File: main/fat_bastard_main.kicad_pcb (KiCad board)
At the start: 2 copper layers, 195 x 50 mm, 54 parts, among them J1 INPUT, J2 TO_LD_12V, J3 TO_LD_IN, J4 TO_LD_GAIN, J5 TO_LD_OUT, J6 12V_IN, J8 FOOTSW, J9 OUTPUT, K1 FINDER-30.22, U1 OPA2134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

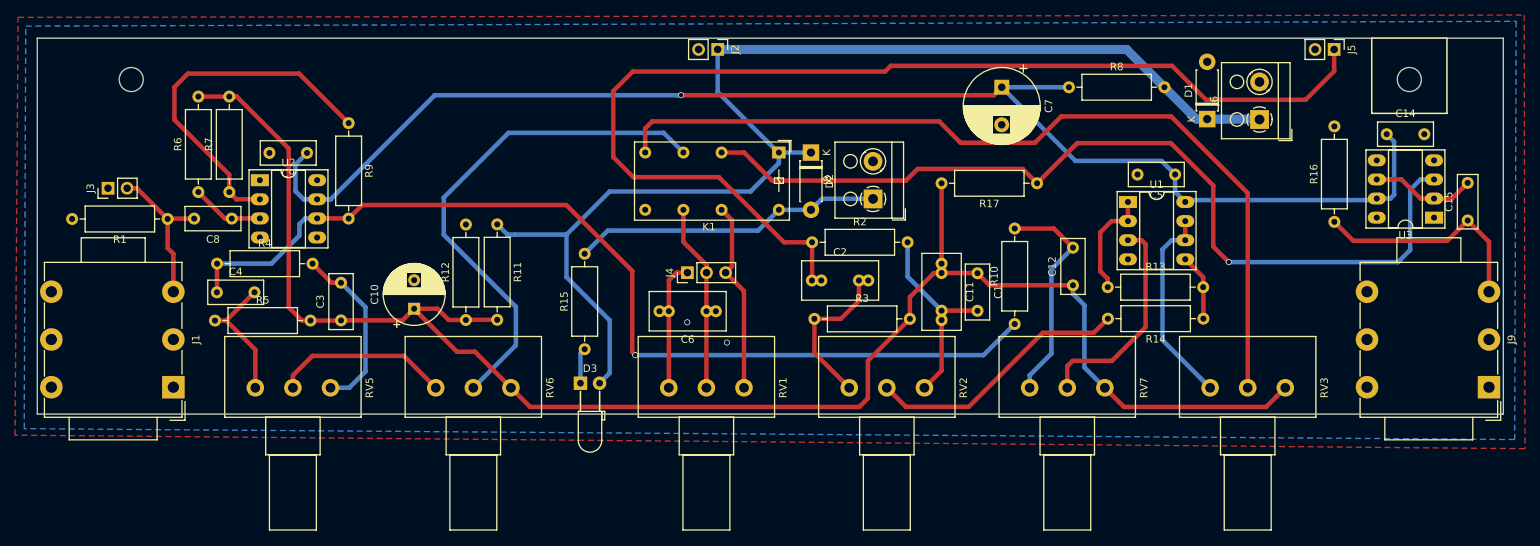
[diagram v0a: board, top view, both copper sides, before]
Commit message: [main] Attenuate lead channel & improve buffering + final PCB
Lead channel has a high output level, while the signal level after the
Depth control is quite low. Therfore, we need to attenuate the lead
channel before trying to mix in the signal coming from the Depth pot.

Additionnally, the output buffer is changed to a make-up gain stage.

With these changes in mind, the PCB design has been completed.
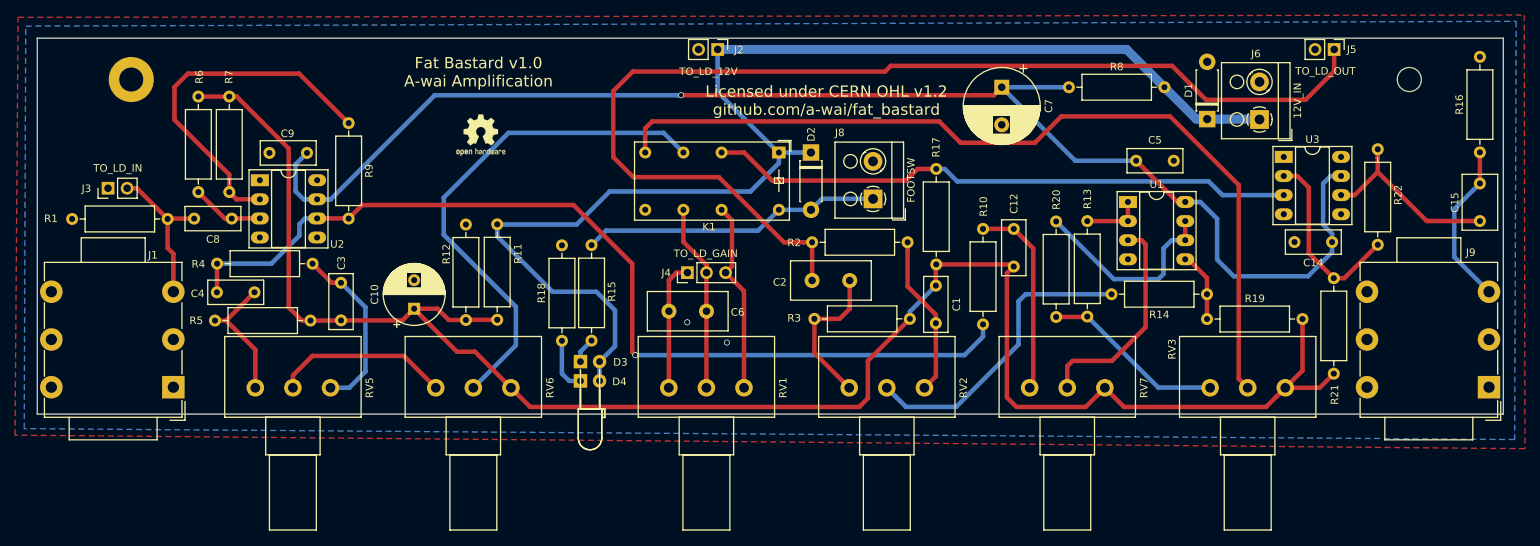
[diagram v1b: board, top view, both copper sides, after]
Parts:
- removed C11: 500p, Capacitor_THT:C_Rect_L10.0mm_W5.0mm_P5.00mm_P7.50mm
- removed the DRILL at (62.5, 65.5)
- added D4: PWR, LED_THT:LED_D3.0mm_Horizontal_O3.81mm_Z2.0mm, F.Cu at (122.3, 105.6)
- added R18: 1.8k, Resistor_THT:R_Axial_DIN0309_L9.0mm_D3.2mm_P12.70mm_Horizontal, F.Cu at (119.8, 100.3)
- added R19: 47k, Resistor_THT:R_Axial_DIN0309_L9.0mm_D3.2mm_P12.70mm_Horizontal, F.Cu at (205.6, 97.4)
- added R20: 10k, Resistor_THT:R_Axial_DIN0309_L9.0mm_D3.2mm_P12.70mm_Horizontal, F.Cu at (185.5, 84.4)
- added R21: 1k, Resistor_THT:R_Axial_DIN0309_L9.0mm_D3.2mm_P12.70mm_Horizontal, F.Cu at (222.5, 104.6)
- added R22: 4.7k, Resistor_THT:R_Axial_DIN0309_L9.0mm_D3.2mm_P12.70mm_Horizontal, F.Cu at (228.3, 87.5)
- added REF**: MountingHole_3.2mm_M3, MountingHole:MountingHole_3.2mm_M3, F.Cu at (62.5, 65.5)
- added REF**: OSHW-Logo2_7.3x6mm_SilkScreen, Symbol:OSHW-Logo2_7.3x6mm_SilkScreen, F.Cu at (109.0, 72.9)
- C1: value 1n -> 1.5n
- C12: value 100n -> 220n
- C15: footprint Capacitor_THT:C_Rect_L7.0mm_W2.5mm_P5.00mm -> Capacitor_THT:C_Rect_L7.2mm_W4.5mm_P5.00mm_FKS2_FKP2_MKS2_MKP2
- C2, C6: footprint Capacitor_THT:C_Rect_L10.0mm_W5.0mm_P5.00mm_P7.50mm -> Capacitor_THT:C_Disc_D10.5mm_W5.0mm_P5.00mm
- D3: value LED -> LEAD; footprint LED_THT:LED_D3.0mm_Horizontal_O3.81mm_Z6.0mm -> LED_THT:LED_D3.0mm_Horizontal_O6.35mm_Z10.0mm
- R10: value 8.2k -> 6.8k
- R13: value 470k -> 10k
- R14: value 470k -> 1M
- R15: value 3.3k -> 1.8k
- R9: value 10k -> 3.9k
- moved U3 21.6 mm to (215.8, 75.8), turned to 0 degrees
- moved R16 21.4 mm to (241.9, 75.2)
- moved C14 16.1 mm to (222.2, 87.1), turned to 180 degrees
- moved R17 13.5 mm to (169.6, 77.4), turned to 270 degrees
- moved C12 8.26 mm to (179.9, 90.4)
- moved C1 5.78 mm to (169.5, 92.9)
- moved C5 5.49 mm to (196.2, 76.3), turned to 0 degrees
- moved C15 5.19 mm to (241.9, 79.3), turned to 270 degrees
- moved R13 4.76 mm to (189.7, 97.0), turned to 90 degrees
- moved R10 4.22 mm to (175.8, 98.1)
- moved R14 3.29 mm to (205.6, 94.1)
- moved D3 2.87 mm to (122.2, 103.0)
- moved R15 1.46 mm to (123.7, 100.2)
- moved C6 1.24 mm to (139.0, 96.3)
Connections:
- R14 pad 1: Net-(R13-Pad2) -> Net-(R14-Pad1)
- RV3 pad 1: Net-(RV3-Pad1) -> Net-(R13-Pad1)
- U1 pad 1: Net-(R13-Pad1) -> Net-(R13-Pad2)
- U1 pad 2: Net-(R13-Pad1) -> Net-(R13-Pad2)
- U1 pad 5: Net-(R13-Pad2) -> Net-(R14-Pad1)
- U1 pad 6: Net-(RV3-Pad1) -> Net-(R20-Pad1)
- U1 pad 7: Net-(RV3-Pad1) -> Net-(R20-Pad1)
- U3 pad 2: Net-(C15-Pad2) -> Net-(R21-Pad2)
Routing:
- net Net-(K1-Pad11): track 120.5 -> 78.4 mm, vias 1 -> 0
- net Net-(RV3-Pad1): track 27.1 -> 0.00 mm
- net Net-(R20-Pad1): track 0.00 -> 27.0 mm
- net Net-(R21-Pad2): track 0.00 -> 25.1 mm
- net GNDS: track 224.9 -> 239.8 mm
- net Net-(C15-Pad2): track 14.0 -> 25.5 mm
- net Net-(R13-Pad1): track 14.5 -> 24.4 mm
- net Net-(R14-Pad1): track 0.00 -> 9.38 mm
- net Net-(C15-Pad1): track 30.5 -> 21.9 mm
- net +12V: track 163.6 -> 171.4 mm
- net Net-(D4-Pad1): track 0.00 -> 7.23 mm
- net Net-(C1-Pad2): track 27.0 -> 21.5 mm
- net Net-(R14-Pad2): track 35.3 -> 40.5 mm
- net Net-(C12-Pad2): track 29.8 -> 26.5 mm
- net Net-(C4-Pad1): track 130.4 -> 127.6 mm
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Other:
- board text added: "Fat Bastard v1.0 A-wai Amplification"
- board text added: "Licensed under CERN OHL v1.2 github.com/a-wai/fat_bastard"

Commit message: Make main-alt PCB the only main PCB
Signed-off-by: Arnaud Ferraris <arnaud.ferraris@gmail.com>
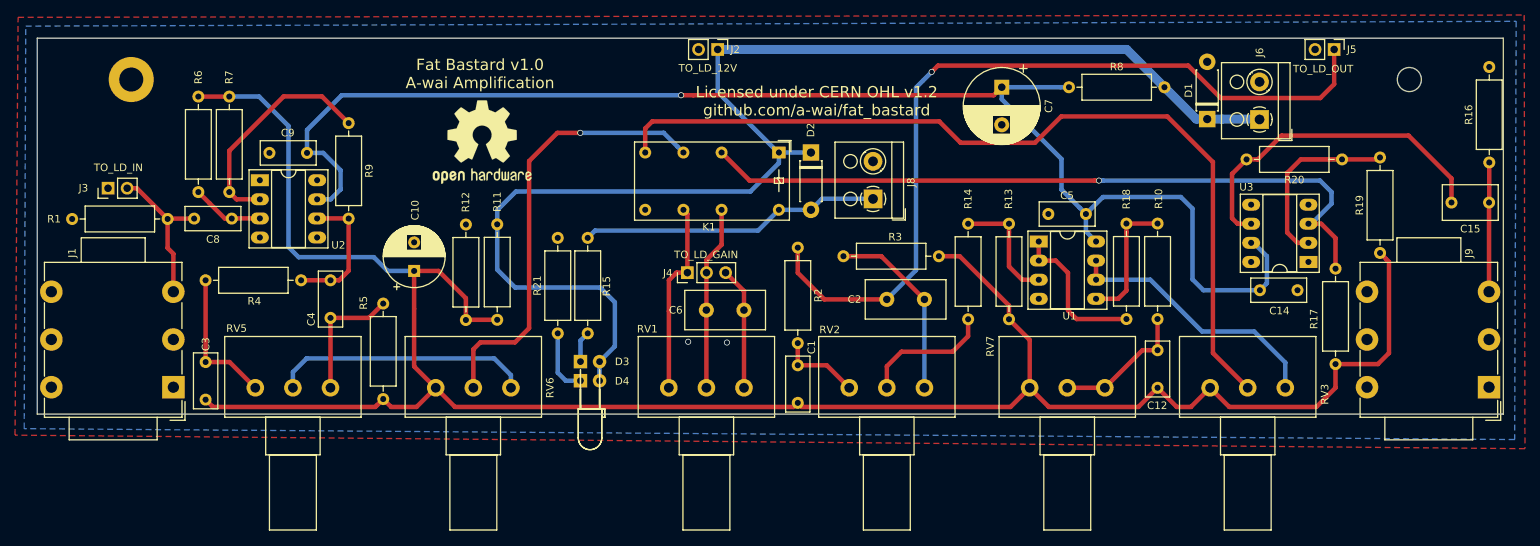
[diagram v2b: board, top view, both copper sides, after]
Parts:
- removed R22: 4.7k, Resistor_THT:R_Axial_DIN0309_L9.0mm_D3.2mm_P12.70mm_Horizontal
- removed the REF** at (62.5, 65.5)
- removed the REF** at (109.0, 72.9)
- added DRILL: MountingHole_3.2mm_M3, MountingHole:MountingHole_3.2mm_M3, F.Cu at (62.5, 65.5)
- added REF**: OSHW-Logo2_14.6x12mm_SilkScreen, Symbol:OSHW-Logo2_14.6x12mm_SilkScreen, F.Cu at (109.2, 73.8)
- C12: value 220n -> 10n
- R1: value 1M -> 2.2M
- R10: value 6.8k -> 33k
- R13: value 10k -> 47k
- R18: value 1.8k -> 330k
- R19: value 47k -> 1k
- R20: value 10k -> 3.3k
- R21: value 1k -> 1.8k
- R9: value 3.9k -> 2.2k
- RV7: value 100k-A -> 1M-A
- moved R21 103.4 mm to (119.2, 99.3)
- moved R18 75.1 mm to (194.9, 97.4)
- moved R17 54.7 mm to (222.7, 90.7)
- moved R20 38.9 mm to (223.5, 76.1), turned to 180 degrees
- moved R14 31.9 mm to (173.8, 97.4), turned to 90 degrees
- moved R10 26.8 mm to (199.0, 84.7), turned to 270 degrees
- moved C12 25.0 mm to (199.0, 106.5)
- moved R19 24.6 mm to (228.6, 88.6), turned to 90 degrees
- moved C1 24.1 mm to (151.2, 108.5), turned to 90 degrees
- moved R5 22.5 mm to (96.0, 95.3), turned to 270 degrees
- moved C3 20.9 mm to (72.4, 108.1)
- moved R13 16.2 mm to (179.2, 84.7), turned to 270 degrees
- moved C4 15.2 mm to (89.0, 92.2), turned to 270 degrees
- moved U3 14.3 mm to (219.1, 89.8), turned to 180 degrees
- moved U1 13.0 mm to (183.2, 87.0)
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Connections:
- J4 pad 1: Net-(C6-Pad2) -> /LD_GND
- J4 pad 3: /LD_GND -> Net-(C6-Pad2)
- K1 pad 21: /LD_GND -> /LD_SIG
- K1 pad 22: /LD_SIG -> /LD_GND
- R10 pad 1: Net-(C4-Pad1) -> Net-(R10-Pad1)
- R13 pad 2: Net-(R13-Pad2) -> GNDS
- R14 pad 2: Net-(R14-Pad2) -> Net-(R13-Pad1)
- R18 pad 1: Net-(D4-Pad1) -> Net-(R18-Pad1)
- R18 pad 2: GND -> Net-(R10-Pad1)
- R19 pad 1: Net-(R14-Pad1) -> GNDS
- R19 pad 2: GNDS -> Net-(R19-Pad2)
- R20 pad 1: Net-(R20-Pad1) -> Net-(R19-Pad2)
- R20 pad 2: Net-(R13-Pad1) -> Net-(C15-Pad2)
- R21 pad 1: GNDS -> Net-(D4-Pad1)
- R21 pad 2: Net-(R21-Pad2) -> GND
- RV1 pad 1: Net-(C6-Pad2) -> /LD_GND
- RV1 pad 3: /LD_GND -> Net-(C6-Pad2)
- RV2 pad 1: Net-(C2-Pad2) -> Net-(C1-Pad2)
- RV2 pad 2: Net-(R14-Pad2) -> Net-(R14-Pad1)
- RV2 pad 3: Net-(C1-Pad2) -> Net-(C2-Pad2)
- RV3 pad 1: Net-(R13-Pad1) -> GNDS
- RV3 pad 3: GNDS -> Net-(RV3-Pad3)
- RV5 pad 1: Net-(C4-Pad2) -> Net-(C3-Pad2)
- RV5 pad 3: Net-(C3-Pad2) -> Net-(C4-Pad2)
- RV6 pad 1: Net-(RV5-Pad2) -> GNDS
- RV6 pad 3: GNDS -> Net-(RV5-Pad2)
- RV7 pad 1: Net-(C12-Pad2) -> GNDS
- RV7 pad 2: Net-(RV7-Pad2) -> Net-(C12-Pad2)
- RV7 pad 3: GNDS -> Net-(C12-Pad2)
- U1 pad 1: Net-(R13-Pad2) -> Net-(R18-Pad1)
- U1 pad 2: Net-(R13-Pad2) -> Net-(R18-Pad1)
- U1 pad 3: Net-(RV7-Pad2) -> Net-(R13-Pad1)
- U1 pad 5: Net-(R14-Pad1) -> Net-(R10-Pad1)
- U1 pad 6: Net-(R20-Pad1) -> Net-(RV3-Pad3)
- U1 pad 7: Net-(R20-Pad1) -> Net-(RV3-Pad3)
- U3 pad 2: Net-(R21-Pad2) -> Net-(R19-Pad2)
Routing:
- net Net-(C4-Pad1): track 127.6 -> 18.0 mm, vias 1 -> 0
- net GNDS: track 239.8 -> 290.3 mm
- net Net-(R14-Pad2): track 40.5 -> 0.00 mm
- net Net-(C2-Pad1): track 148.6 -> 110.4 mm, vias 0 -> 1
- net Net-(RV3-Pad3): track 0.00 -> 35.6 mm
- net Net-(R19-Pad2): track 0.00 -> 29.9 mm
- net Net-(RV7-Pad2): track 29.0 -> 0.00 mm
- net Net-(R20-Pad1): track 27.0 -> 0.00 mm
- net Net-(R21-Pad2): track 25.1 -> 0.00 mm
- net Net-(R18-Pad1): track 0.00 -> 20.3 mm
- net Net-(C15-Pad2): track 25.5 -> 45.6 mm
- net Net-(K1-Pad11): track 78.4 -> 97.5 mm, vias 0 -> 1
- net Net-(R7-Pad1): track 48.1 -> 30.3 mm
- net Net-(R10-Pad1): track 0.00 -> 17.5 mm
- net Net-(RV5-Pad2): track 23.5 -> 34.4 mm
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
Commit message: Add bright cap, DI out & improve routing
* Add bright cap on clean channel
* Add DI out pin header
* Change connections to improve routing
* Connect pin 1 of each pin header & terminal block to GND for improved
  consistency
* Improve overall routing to avoid vias

Signed-off-by: Arnaud Ferraris <arnaud.ferraris@gmail.com>
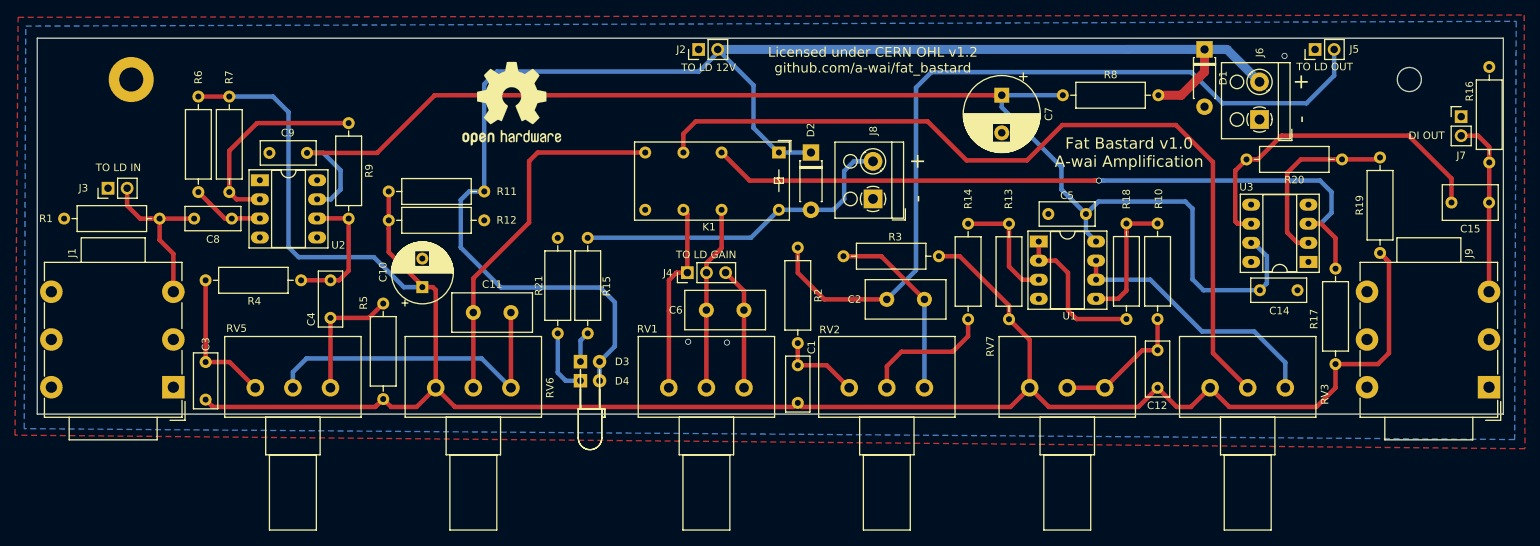
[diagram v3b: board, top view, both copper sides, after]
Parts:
- added C11: 100p, Capacitor_THT:C_Disc_D10.5mm_W5.0mm_P5.00mm, F.Cu at (108.0, 96.5)
- added J7: DI OUT, Connector_PinHeader_2.54mm:PinHeader_1x02_P2.54mm_Vertical, F.Cu at (239.4, 70.4)
- J2: value TO_LD_12V -> TO LD 12V
- J3: value TO_LD_IN -> TO LD IN
- J4: value TO_LD_GAIN -> TO LD GAIN
- J5: value TO_LD_OUT -> TO LD OUT
- J6: value 12V_IN -> 12V IN
- moved R12 16.8 mm to (96.7, 84.2), turned to 0 degrees
- moved D1 9.28 mm to (205.3, 61.5), turned to 270 degrees
- moved REF** 6.45 mm to (113.1, 68.7)
- moved R11 4.70 mm to (109.4, 80.4), turned to 180 degrees
- moved J2 2.54 mm to (138.0, 61.5), turned to 90 degrees
- moved J5 2.54 mm to (220.0, 61.5), turned to 90 degrees
- moved C10 2.42 mm to (101.2, 93.1)
- moved R8 1.34 mm to (186.4, 67.6)
- moved R1 1.07 mm to (66.3, 84.0)
- moved C7 1.07 mm to (178.3, 67.6)
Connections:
- J2 pad 1: +12V -> GND
- J2 pad 2: GND -> +12V
- J5 pad 1: Net-(C2-Pad1) -> (no net)
- J5 pad 2: (no net) -> Net-(C2-Pad1)
- J6 pad 1: +12V -> GND
- J6 pad 2: GND -> +12V
- J8 pad 1: Net-(D2-Pad2) -> GND
- J8 pad 2: GND -> Net-(D2-Pad2)
- K1 pad 14: Net-(K1-Pad14) -> Net-(C11-Pad1)
- RV3 pad 2: Net-(K1-Pad14) -> Net-(K1-Pad12)
- RV6 pad 2: Net-(K1-Pad12) -> Net-(C11-Pad1)
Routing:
- net Net-(K1-Pad14): track 116.2 -> 0.00 mm
- net Net-(K1-Pad12): track 59.1 -> 111.7 mm, vias 1 -> 0
- net Net-(C11-Pad1): track 0.00 -> 49.1 mm
- net +12V: track 175.6 -> 197.9 mm
- net Net-(C11-Pad2): track 34.4 -> 43.5 mm
- net Net-(C15-Pad1): track 17.2 -> 23.6 mm
- net Net-(R19-Pad2): track 29.9 -> 24.5 mm
- net VCC: track 186.6 -> 182.0 mm, vias 1 -> 0
- net Net-(D2-Pad2): track 40.1 -> 44.4 mm
- net Net-(R7-Pad1): track 30.3 -> 27.4 mm
- net Net-(C8-Pad2): track 20.6 -> 22.4 mm
- net Net-(C2-Pad1): track 110.4 -> 109.6 mm, vias 1 -> 0
- net Net-(K1-Pad11): track 97.5 -> 98.2 mm
- net GND: vias 2 -> 3
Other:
- board text added: "+"
- board text added: "-"

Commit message: [main] Fix channel switching
Due to changing the schematics layout in the previous version, default
channel is lead and is muted.

This commit restores the original layout and fixes the corresponding
traces.

Signed-off-by: Arnaud Ferraris <arnaud.ferraris@gmail.com>
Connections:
- K1 pad 12: Net-(K1-Pad12) -> Net-(C11-Pad1)
- K1 pad 14: Net-(C11-Pad1) -> Net-(K1-Pad14)
- RV3 pad 2: Net-(K1-Pad12) -> Net-(K1-Pad14)
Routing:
- net Net-(K1-Pad14): track 0.00 -> 116.7 mm
- net Net-(K1-Pad12): track 111.7 -> 0.00 mm
- net Net-(C11-Pad1): track 49.1 -> 50.5 mm
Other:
- board text added: "Fat Bastard v1.1 A-wai Amplification"
- board text removed: "Fat Bastard v1.0 A-wai Amplification"

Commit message: Add alternate component values for guitar
In its original form, this preamp could very well be used with a guitar,
providing a rather tight and modern sound.

This patch adds alternate values, designed for use with guitar,
resulting in a warmer, fuller, stoner/rock guitar tone.

Signed-off-by: Arnaud Ferraris <arnaud.ferraris@gmail.com>
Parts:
- C11: value 100p -> not fitted
- C12: value 10n -> 15n
- C6: value 500p -> not fitted
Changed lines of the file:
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@@
       (effects (font (size 1 1) (thickness 0.15)))
     )
-    (fp_text value 10n (at 2.5 2.75 90) (layer F.Fab)
+    (fp_text value 15n (at 2.5 2.75 90) (layer F.Fab)
       (effects (font (size 1 1) (thickness 0.15)))
     )
@@
       (effects (font (size 1 1) (thickness 0.15)))
     )
-    (fp_text value 500p (at 2.5 3.75) (layer F.Fab)
+    (fp_text value "not fitted" (at 2.5 3.75) (layer F.Fab)
       (effects (font (size 1 1) (thickness 0.15)))
     )
@@
       (effects (font (size 1 1) (thickness 0.15)))
     )
-    (fp_text value 100p (at 2.5 3.75) (layer F.Fab)
-      (effects (font (size 1 1) (thickness 0.15)))
-    )
+    (fp_text value "not fitted" (at 2.5 3.75) (layer F.Fab)
+      (effects (font (size 1 1) (thickness 0.15)))
+    )
